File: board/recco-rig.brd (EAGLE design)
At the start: 60.2 x 60 mm, 34 parts, among them IC1 LM386, IC2 TL072-OPAMP, P10-LINE-IN PIN-HEADER-2PIN, P2-SPKR-OUT PIN-HEADER-3PIN, P3-SPKR-MIC-IN PIN-HEADER-4PIN

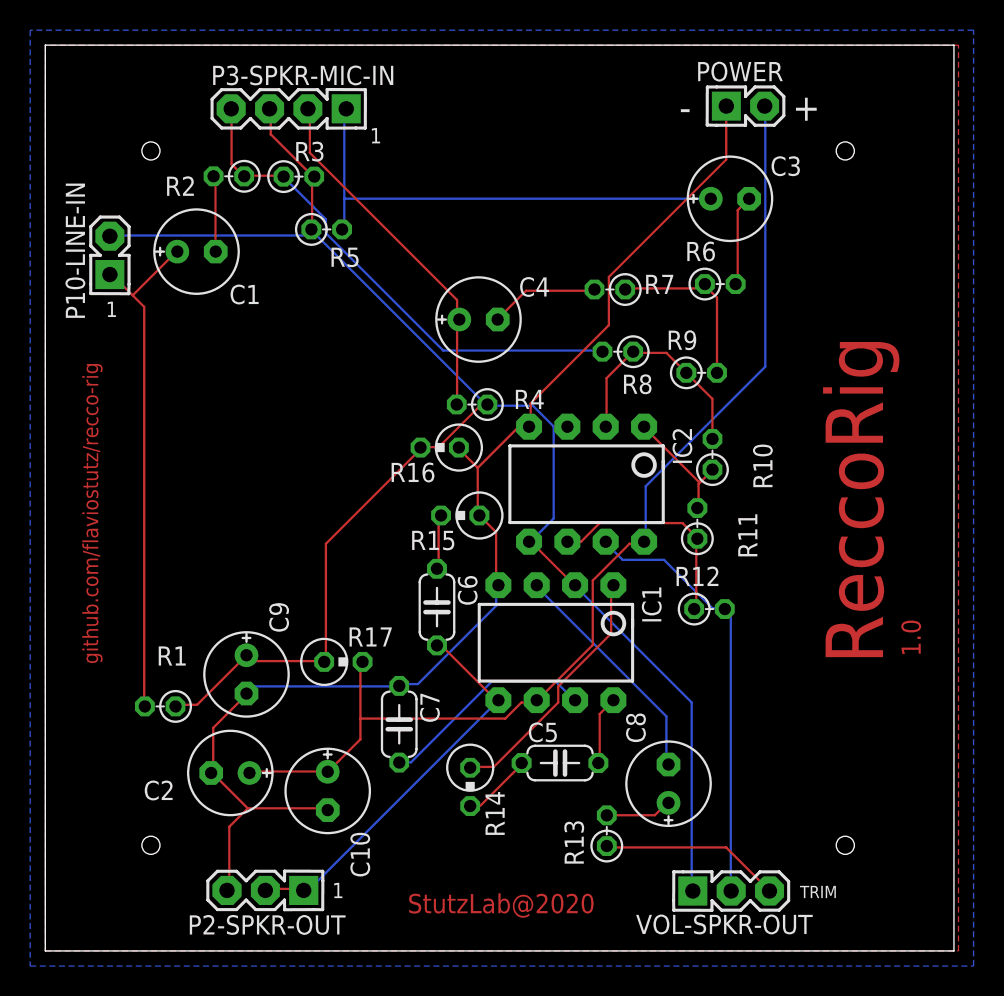
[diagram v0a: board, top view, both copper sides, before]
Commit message: physical board and mic protection
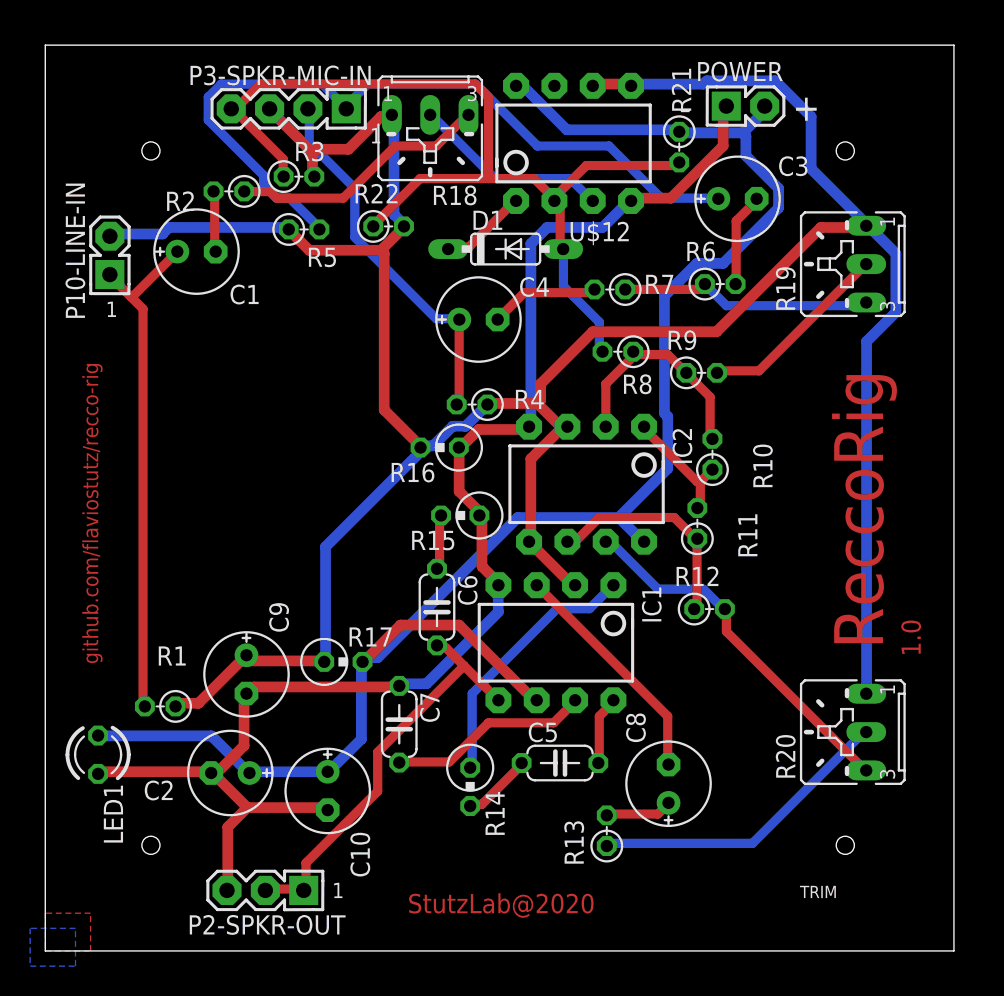
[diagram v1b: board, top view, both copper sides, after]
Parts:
- removed VOL-SPKR-OUT: HEADPHONE-VOLUME-KNOB, stutz-components-library:PIN-HEADER-3PIN
- added D1: 1N4148DO35-7, diode:DO35-7
- added LED1: TLLG4400, led:LED3MM
- added R18, R19: 10k log, pot:B25U
- added R20: 10k, pot:B25U
- added R21: 10k, stutz-components-library:RESISTOR-V1
- added R22: 1k, stutz-components-library:RESISTOR-V1
- added U$12: TL072-OPAMP, stutz-components-library:PDIP-8PIN
- C6: value 0.05uF -> 47pF
- R16, R17: value 100k -> 1k
- moved R5 1.50 mm to (17.4, 47.8)
- moved R2 1.00 mm to (11.9, 50.3)
- moved C3 0.50 mm to (45.9, 49.8)
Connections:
- new net N$18: R19.E, R6.1, R7.1
- new net N$19: R18.S, U$12.3
- new net N$21: D1.C, U$12.1
- new net N$9: R18.E, R2.1
- net +9V: now also LED1.A, R21.1, U$12.8
- net GND: now also LED1.K, U$12.4
- net HEADPHONE-OUTPUT: now also R20.E; no longer VOL-SPKR-OUT.2
- net N$11: now also R20.S; no longer VOL-SPKR-OUT.3
- net P3-MICIN-MONO: now also D1.A, R21.2, R22.1, U$12.2; no longer R2.1
- net P3-SPKROUT-MONO: now also R19.S; no longer R6.1, R7.1
- net VGND: now also R18.A, R19.A, R20.A, R22.2, U$12.5, U$12.6; no longer VOL-SPKR-OUT.1
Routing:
- net VGND: track 115.4 -> 192.7 mm
- net +9V: track 72.0 -> 113.1 mm
- net P3-MICIN-MONO: track 34.0 -> 64.3 mm
- net N$8: track 32.5 -> 51.1 mm
- net N$9: track 0.00 -> 17.3 mm
- net N$18: track 0.00 -> 16.8 mm
- net N$19: track 0.00 -> 13.1 mm
- net GND: track 82.9 -> 95.4 mm
- net N$11: track 12.0 -> 20.3 mm
- net N$21: track 0.00 -> 5.83 mm
- net HEADPHONE-OUTPUT: track 28.6 -> 24.4 mm
- net P3-SPKROUT-MONO: track 11.6 -> 12.8 mm
- net N$15: track 26.4 -> 27.4 mm
- net N$16: track 14.4 -> 13.4 mm
- net N$1: track 5.05 -> 4.08 mm
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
